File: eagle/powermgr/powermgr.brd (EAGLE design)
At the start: 88.9 x 38.1 mm, 36 parts, among them IC1 PIC16F1455TSSOP-14, IC2 4027D, IC3 MCP1804, IC4 ACS756, Q1 BSS123, Q2 BSS123, X1 10104111-0001LF

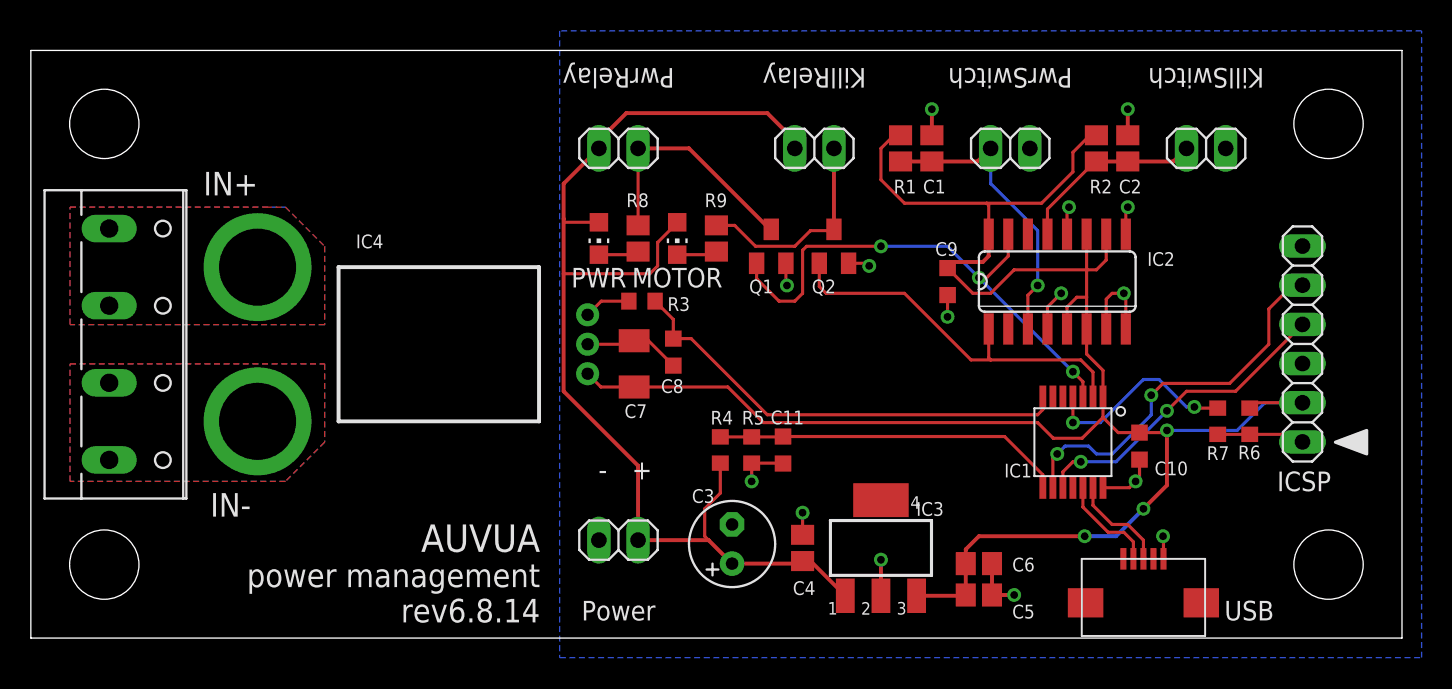
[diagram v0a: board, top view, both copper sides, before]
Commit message: Added schmitt trigger to switch inputs. Sent rev 6.16.14 for production.
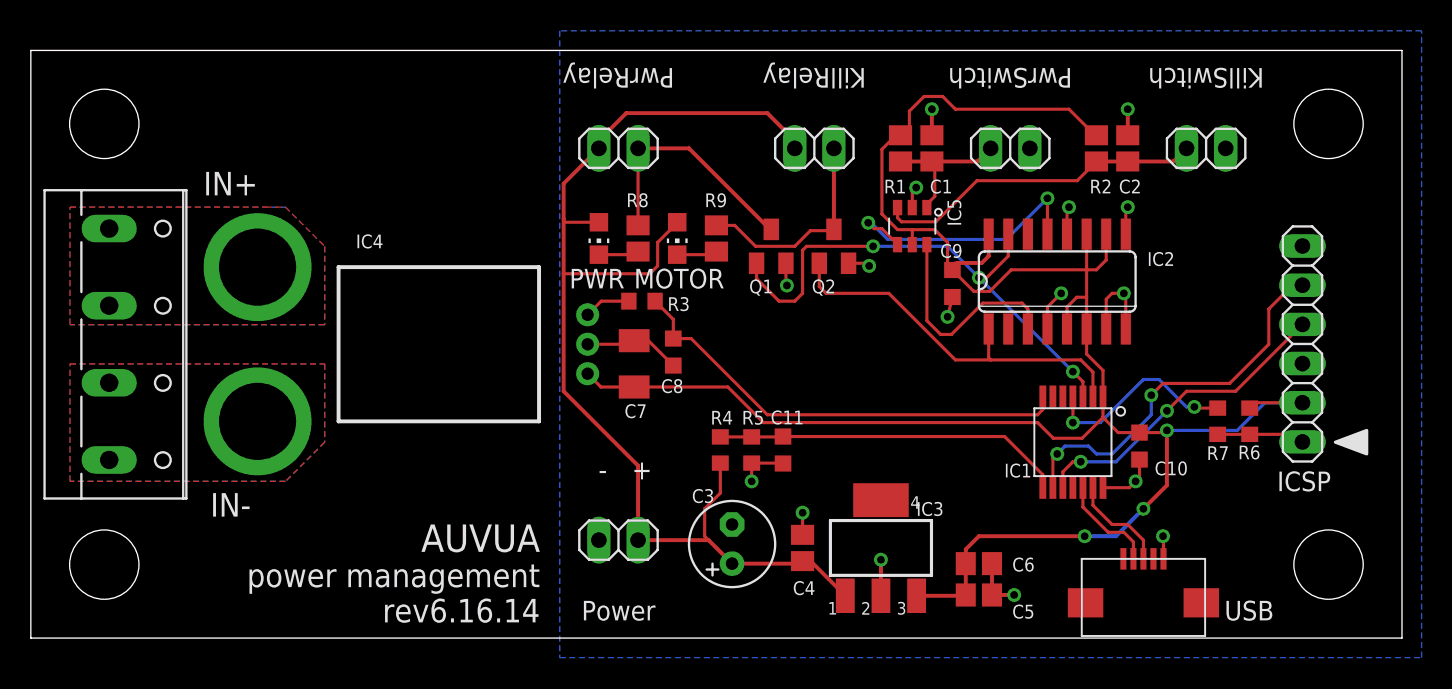
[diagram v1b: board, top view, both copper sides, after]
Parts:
- added IC5: 74HC2G14, custom:TSSOP-6
- D1: value (none) -> PWR
- D2: value (none) -> MOTOR
- moved C9 0.34 mm to (59.8, 23.0)
- renumbered MOTOR to D2, PWR to D1
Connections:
- removed net N$2: C2.1, IC2.13, JP2.1, R2.1
- new net N$15: C2.1, IC5.3, JP2.1, R2.1
- new net N$17: IC2.3, IC5.6
- new net N$18: IC2.13, IC5.4
- net +5V: now also IC5.5
- net GND: now also IC5.2
- net N$1: now also IC5.1; no longer IC2.3
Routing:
- net N$15: track 0.00 -> 21.6 mm
- net N$18: track 0.00 -> 18.0 mm, vias 0 -> 2
- net N$17: track 0.00 -> 14.1 mm
- net N$2: track 12.3 -> 0.00 mm
- net N$1: track 19.4 -> 9.59 mm, vias 1 -> 0
- net +5V: track 134.3 -> 139.8 mm
- net GND: track 41.6 -> 42.9 mm, vias 15 -> 16
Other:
- board text added: "MOTOR"
- board text added: "PWR"
- board text added: "rev6.16.14"
- board text removed: "rev6.8.14"
